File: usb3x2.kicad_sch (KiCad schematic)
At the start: 102 parts

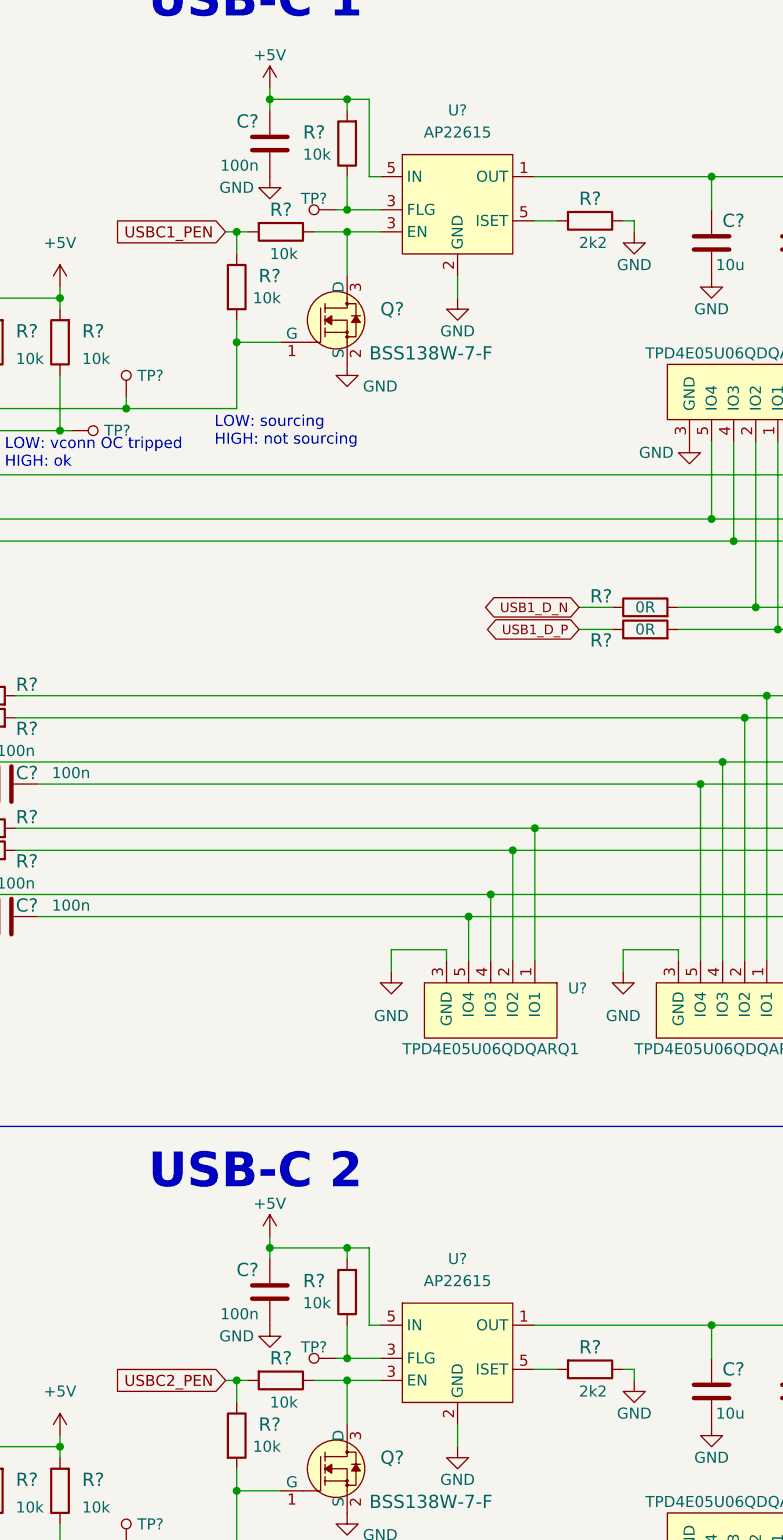
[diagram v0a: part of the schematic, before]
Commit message: Update AP22615 symbols
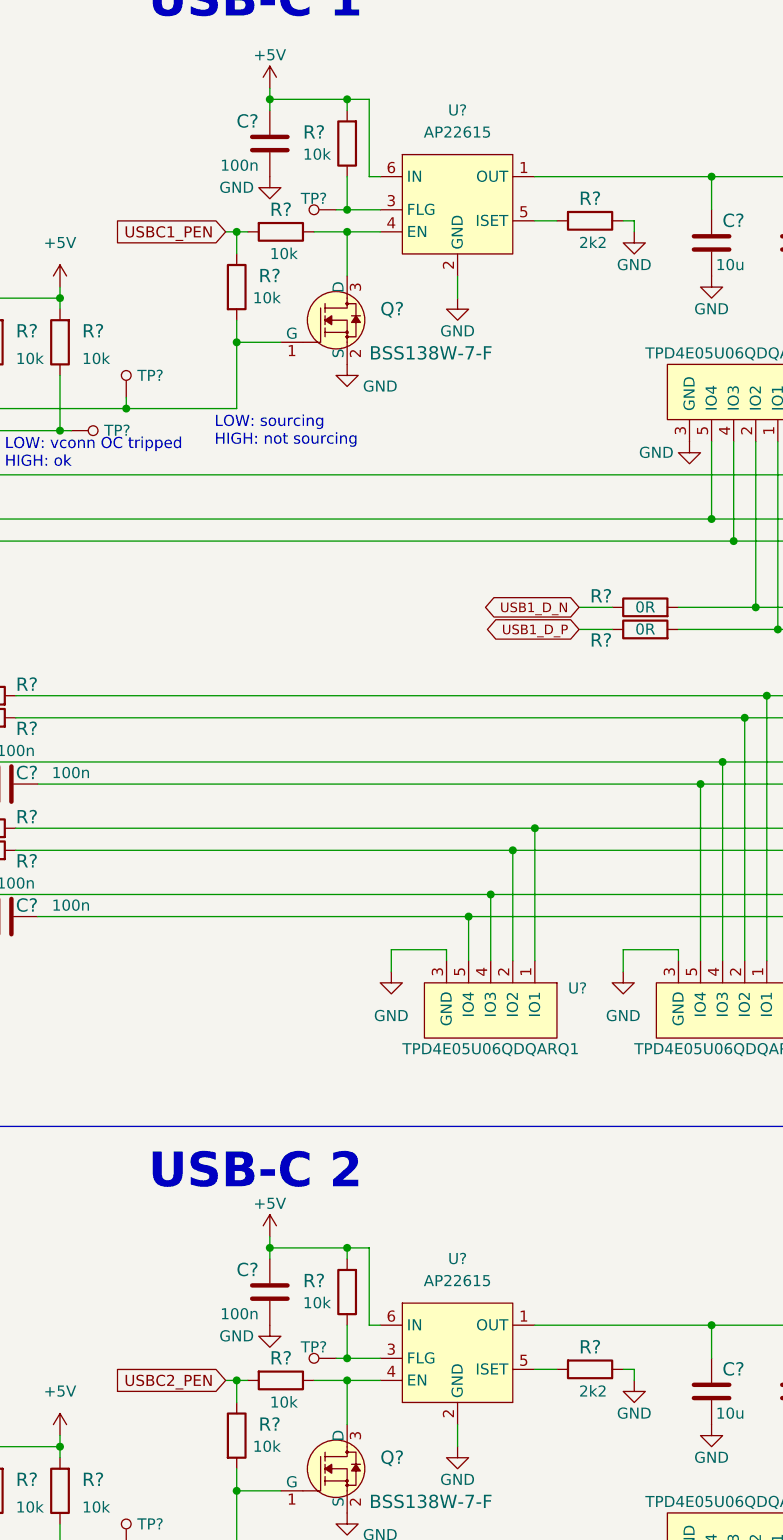
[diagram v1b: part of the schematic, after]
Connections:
- net +5V: now also U?.6 (IN), U?.6 (IN); no longer U?.5 (ISET), U?.5 (ISET)
- net at Q?.3 (D), R?.1: now also U?.4 (EN); no longer U?.3 (FLG) (x2)
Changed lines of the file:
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@@
     (pin "1")
   )
-  (symbol (lib_id "antmicroPMICPowerDistributionSwitchesLoadDrivers:AP22615") (at 224.79 39.37 0) (unit 1)
+  (symbol (lib_name "AP22615_1") (lib_id "antmicroPMICPowerDistributionSwitchesLoadDrivers:AP22615") (at 224.79 39.37 0) (unit 1)
     (in_bom yes) (on_board yes) (fields_autoplaced)
     (property "Reference" "U?" (id 0) (at 224.79 31.75 0))
@@
     (pin "2")
     (pin "3")
-    (pin "3")
+    (pin "4")
     (pin "5")
-    (pin "5")
+    (pin "6")
   )
   (symbol (lib_id "power:GND") (at 264.16 182.88 0) (mirror y) (unit 1)
@@
     (pin "2")
     (pin "3")
-    (pin "3")
+    (pin "4")
     (pin "5")
-    (pin "5")
+    (pin "6")
   )
   (symbol (lib_id "antmicroResistors0402:R_10k_0402") (at 91.44 205.74 270) (unit 1)

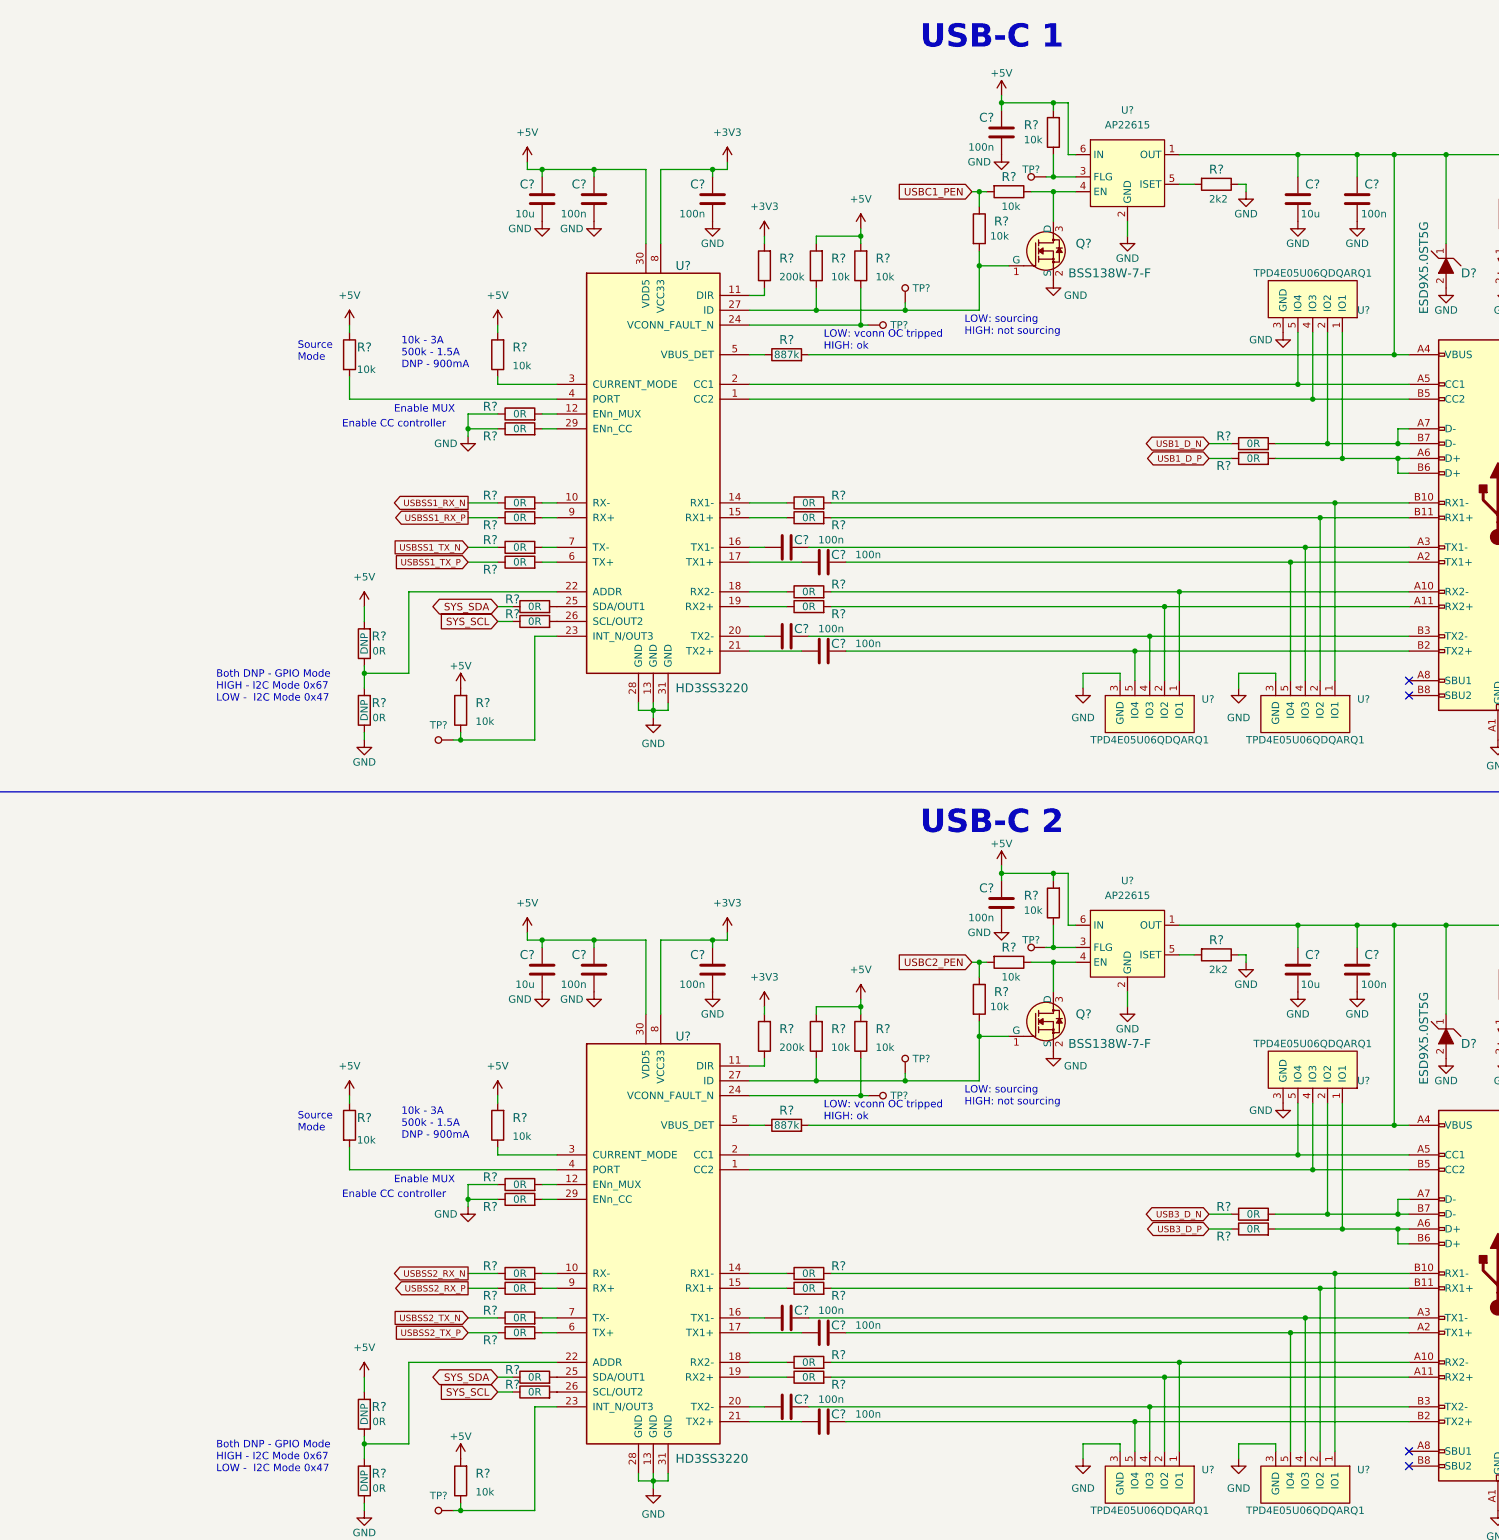
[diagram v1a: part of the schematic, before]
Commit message: Add inter-sheets references
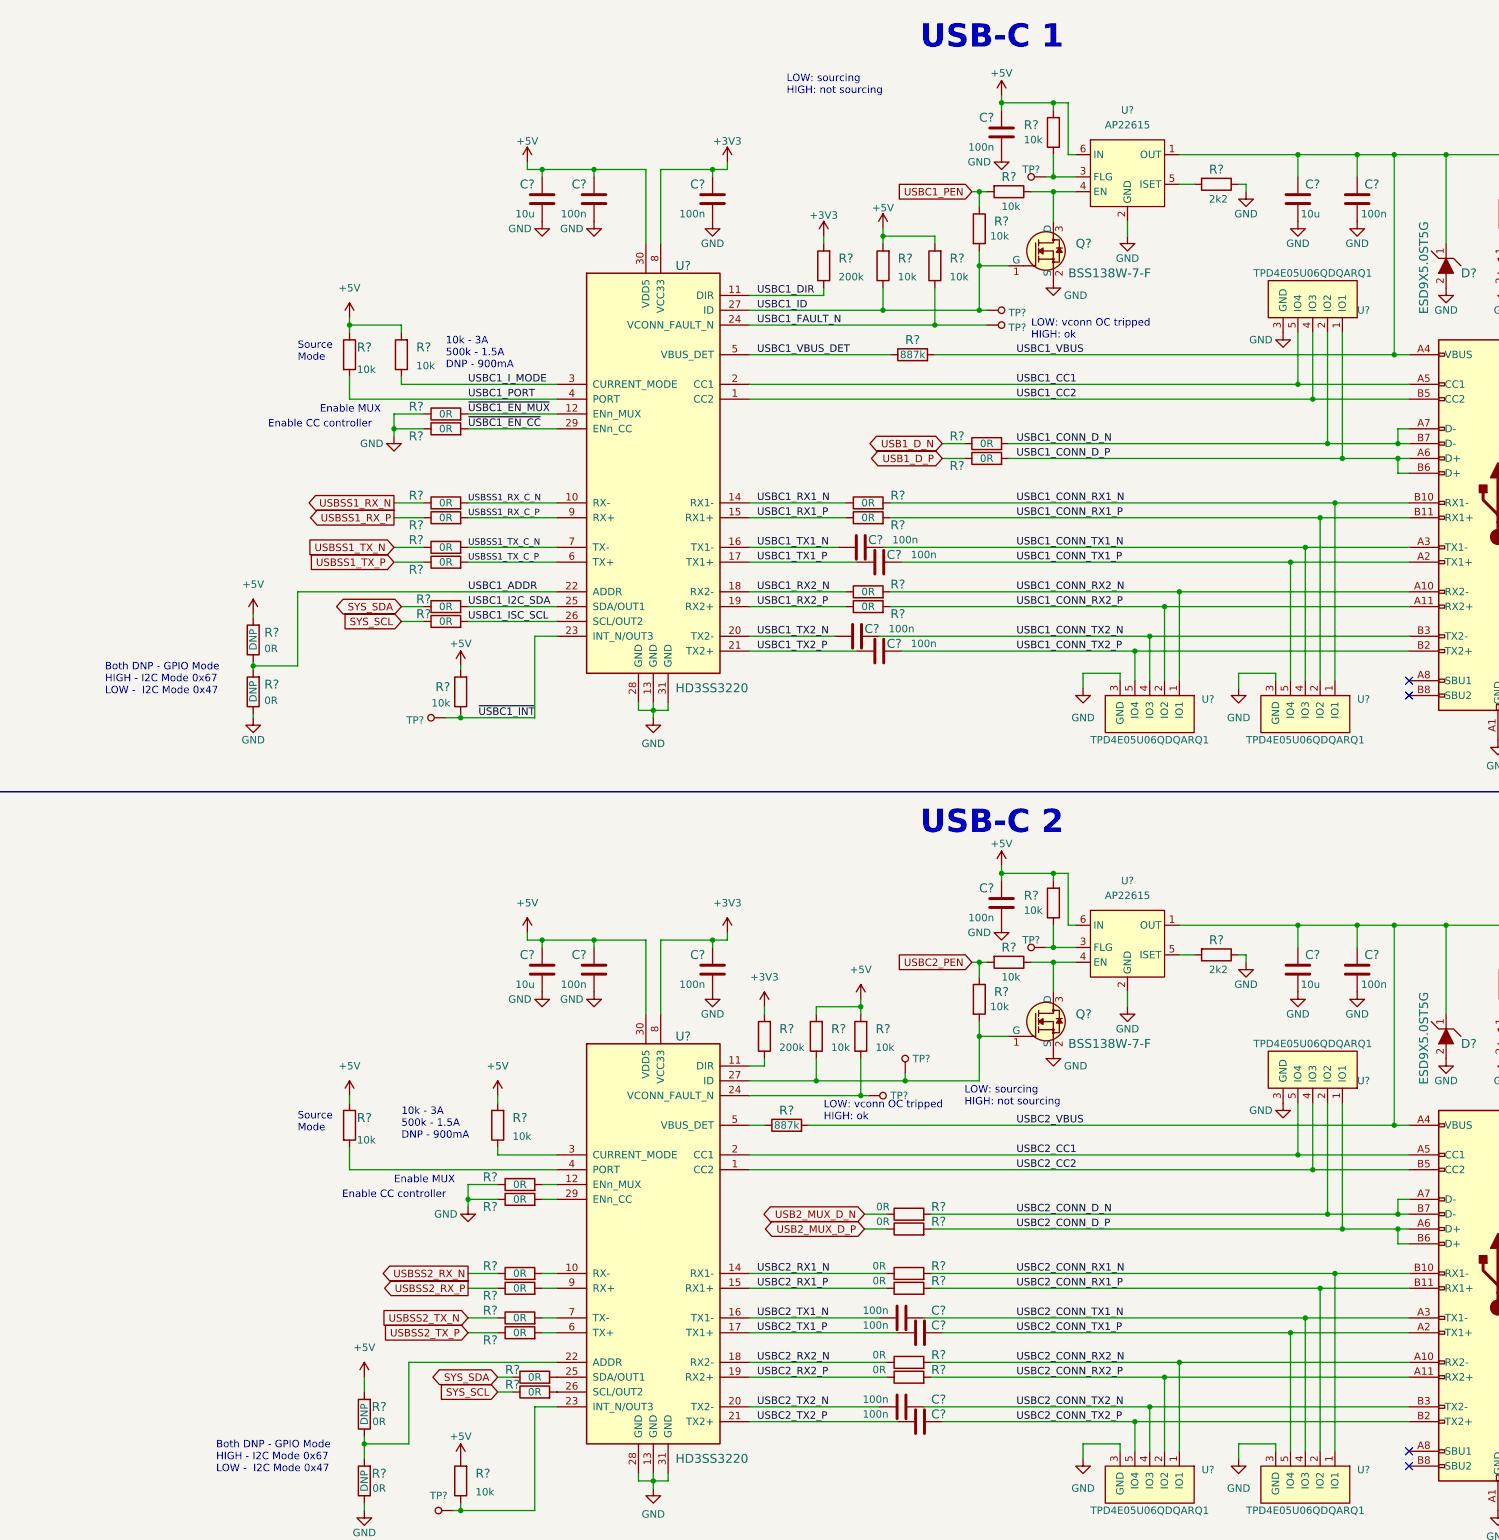
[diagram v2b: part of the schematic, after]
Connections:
- net USBC1_CC2: now reaches J?.B5 (CC2), U?.1 (CC2), U?.4 (IO3), U?.7 (IO3)
- net USBSS1_RX_C_N: now reaches R?.2, U?.10 (RX-)
- net USBC1_DIR: now reaches R?.1, U?.11 (DIR)
- net ~{USBC1_EN_MUX}: now reaches R?.2, U?.12 (ENn_MUX)
- net USBC1_RX1_N: now reaches R?.1, U?.14 (RX1-)
- net USBC1_RX1_P: now reaches R?.1, U?.15 (RX1+)
- net USBC1_TX1_N: now reaches C?.1, U?.16 (TX1-)
- net USBC1_TX1_P: now reaches C?.1, U?.17 (TX1+)
- net USBC1_RX2_N: now reaches R?.1, U?.18 (RX2-)
- net USBC1_RX2_P: now reaches R?.1, U?.19 (RX2+)
- net USBC1_CC1: now reaches J?.A5 (CC1), U?.2 (CC1), U?.5 (IO4), U?.6 (IO4)
- net USBC1_TX2_N: now reaches C?.1, U?.20 (TX2-)
- net USBC1_TX2_P: now reaches C?.1, U?.21 (TX2+)
- net USBC1_ADDR: now reaches R?.1, R?.2, U?.22 (ADDR)
- net ~{USBC1_INT}: now reaches R?.1, TP?.1, U?.23 (INT_N/OUT3)
- net USBC1_FAULT_N: now reaches R?.1, TP?.1, U?.24 (VCONN_FAULT_N)
- net USBC1_I2C_SDA: now reaches R?.2, U?.25 (SDA/OUT1)
- net USBC1_ISC_SCL: now reaches R?.2, U?.26 (SCL/OUT2)
- net USBC1_ID: now reaches Q?.1 (G), R?.1, R?.2, TP?.1, U?.27 (ID)
- net ~{USBC1_EN_CC}: now reaches R?.2, U?.29 (ENn_CC)
- net USBC1_I_MODE: now reaches R?.1, U?.3 (CURRENT_MODE)
- net USBC1_PORT: now reaches R?.2, U?.4 (PORT)
- net USBC1_VBUS_DET: now reaches R?.1, U?.5 (VBUS_DET)
- net USBSS1_TX_C_P: now reaches R?.2, U?.6 (TX+)
- net USBSS1_TX_C_N: now reaches R?.2, U?.7 (TX-)
- net USBSS1_RX_C_P: now reaches R?.2, U?.9 (RX+)
- net USBC1_CONN_RX2_N: now reaches J?.A10 (RX2-), R?.2, U?.1 (IO1), U?.10 (IO1)
- net USBC1_VBUS: now reaches C?.1, C?.1, D?.1, J?.A4 (VBUS), J?.A9 (VBUS), J?.B4 (VBUS), J?.B9 (VBUS), R?.2, R?.2, U?.1 (OUT)
- net USBC2_VBUS: now reaches C?.1, C?.1, D?.1, J?.A4 (VBUS), J?.A9 (VBUS), J?.B4 (VBUS), J?.B9 (VBUS), R?.2, R?.2, U?.1 (OUT)
- net USBC2_CONN_RX1_N: now reaches J?.B10 (RX1-), R?.2, U?.1 (IO1), U?.10 (IO1)
- net USBC2_CONN_RX1_P: now reaches J?.B11 (RX1+), R?.2, U?.2 (IO2), U?.9 (IO2)
- net USBC2_CONN_TX1_N: now reaches C?.2, J?.A3 (TX1-), U?.4 (IO3), U?.7 (IO3)
- net USBC2_CONN_TX1_P: now reaches C?.2, J?.A2 (TX1+), U?.5 (IO4), U?.6 (IO4)
- net USBC2_TX2_P: now reaches C?.1, U?.21 (TX2+)
- net USBC2_CONN_TX2_P: now reaches C?.2, J?.B2 (TX2+), U?.5 (IO4), U?.6 (IO4)
- net USBC2_CONN_RX2_N: now reaches J?.A10 (RX2-), R?.2, U?.1 (IO1), U?.10 (IO1)
- net USBC2_CONN_RX2_P: now reaches J?.A11 (RX2+), R?.2, U?.2 (IO2), U?.9 (IO2)
- net USBC2_CONN_TX2_N: now reaches C?.2, J?.B3 (TX2-), U?.4 (IO3), U?.7 (IO3)
- net USBC2_CONN_D_N: now reaches J?.A7 (D-), J?.B7 (D-), R?.2, U?.2 (IO2), U?.9 (IO2)
- net USBC1_CONN_D_P: now reaches J?.A6 (D+), J?.B6 (D+), R?.2, U?.1 (IO1), U?.10 (IO1)
- net USBC2_CC2: now reaches J?.B5 (CC2), U?.1 (CC2), U?.4 (IO3), U?.7 (IO3)
- net USBC2_RX1_N: now reaches R?.1, U?.14 (RX1-)
- net USBC2_RX1_P: now reaches R?.1, U?.15 (RX1+)
- net USBC2_TX1_N: now reaches C?.1, U?.16 (TX1-)
- net USBC2_TX1_P: now reaches C?.1, U?.17 (TX1+)
- net USBC2_RX2_N: now reaches R?.1, U?.18 (RX2-)
- net USBC2_RX2_P: now reaches R?.1, U?.19 (RX2+)
- net USBC2_CC1: now reaches J?.A5 (CC1), U?.2 (CC1), U?.5 (IO4), U?.6 (IO4)
- net USBC2_TX2_N: now reaches C?.1, U?.20 (TX2-)
- net USBC1_CONN_TX1_P: now reaches C?.2, J?.A2 (TX1+), U?.5 (IO4), U?.6 (IO4)
- net USBC1_CONN_RX2_P: now reaches J?.A11 (RX2+), R?.2, U?.2 (IO2), U?.9 (IO2)
- net USBC1_CONN_TX2_N: now reaches C?.2, J?.B3 (TX2-), U?.4 (IO3), U?.7 (IO3)
- net USBC1_CONN_TX2_P: now reaches C?.2, J?.B2 (TX2+), U?.5 (IO4), U?.6 (IO4)
- net USBC1_CONN_TX1_N: now reaches C?.2, J?.A3 (TX1-), U?.4 (IO3), U?.7 (IO3)
- net USBC1_CONN_D_N: now reaches J?.A7 (D-), J?.B7 (D-), R?.2, U?.2 (IO2), U?.9 (IO2)
- net USBC1_CONN_RX1_N: now reaches J?.B10 (RX1-), R?.2, U?.1 (IO1), U?.10 (IO1)
- net USBC1_CONN_RX1_P: now reaches J?.B11 (RX1+), R?.2, U?.2 (IO2), U?.9 (IO2)
- net USBC2_CONN_D_P: now reaches J?.A6 (D+), J?.B6 (D+), R?.2, U?.1 (IO1), U?.10 (IO1)
- net USB3_D_N renamed USB2_MUX_D_N
- net USB3_D_P renamed USB2_MUX_D_P
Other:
- moved on the sheet: C?, R?, TP?
